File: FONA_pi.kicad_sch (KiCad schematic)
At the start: 26 parts, among them J1 Conn_01x20_Socket, J10 Conn_01x04_Pin, J11 Conn_01x20_Socket, J12 Conn_01x20_Socket, J13 Conn_01x06_Socket, J14 Conn_01x06_Socket, J15 Conn_01x06_Socket, J16 Conn_01x06_Socket, J17 Conn_01x06_Socket, J2 Conn_02x20_Odd_Even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

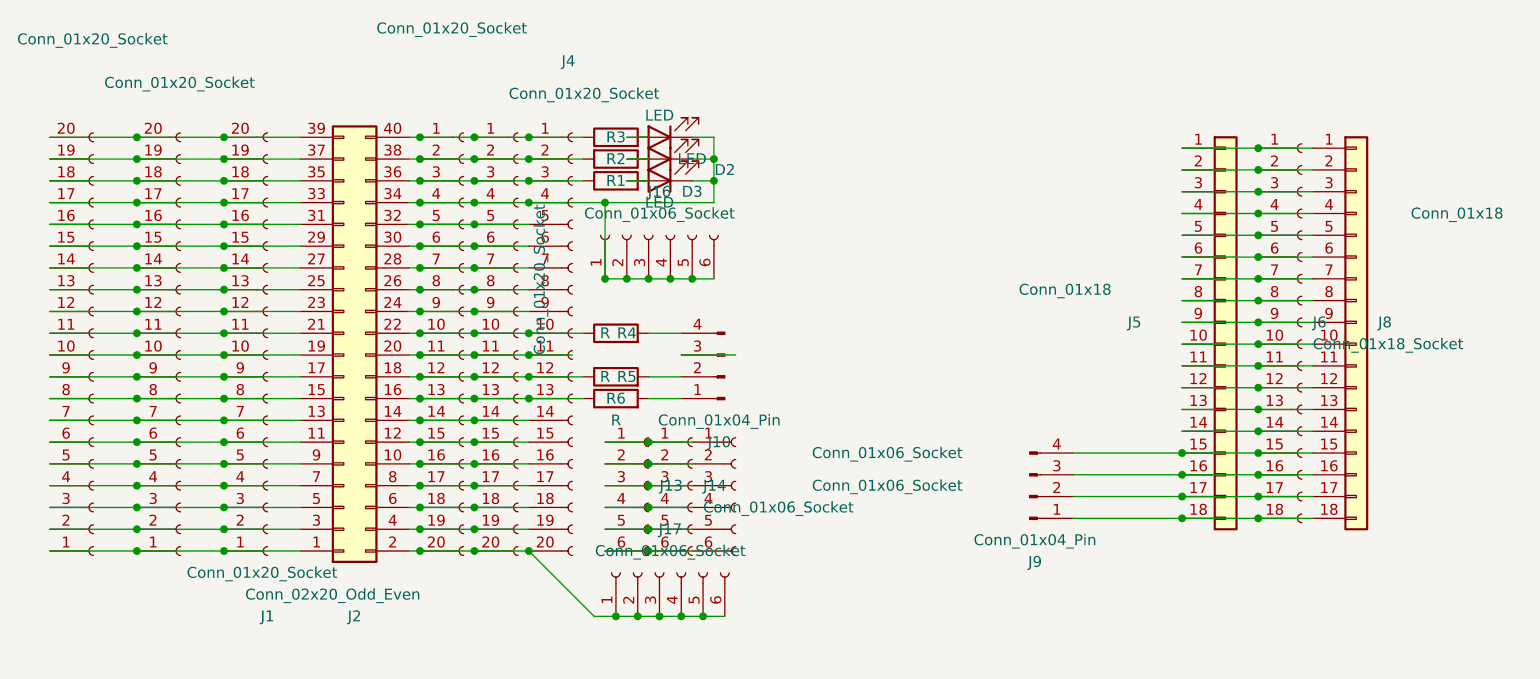
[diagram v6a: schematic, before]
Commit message: Added solder jumpers, ran them to GPIO pins.  Connected FONA pins to Pi, UART RX/TX, RI, NS, PS, etc to various GPIOs
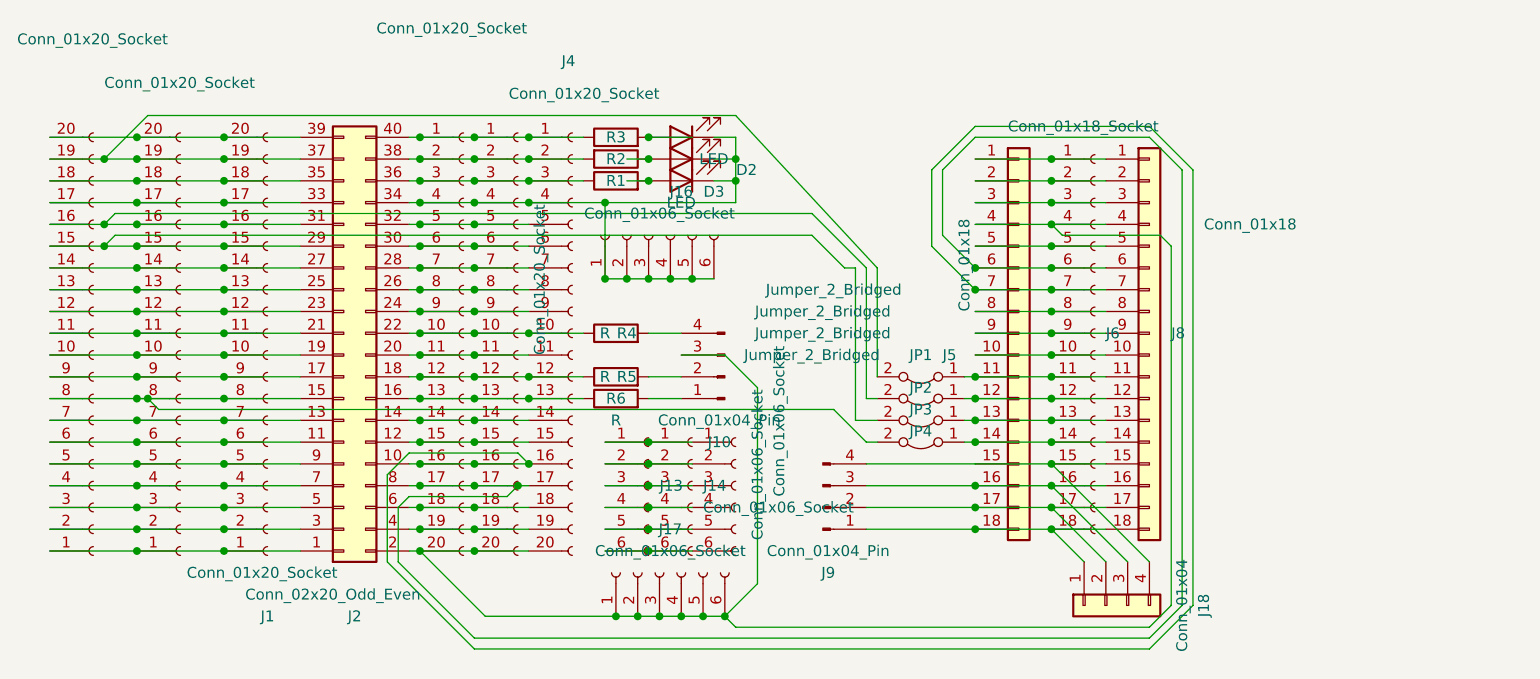
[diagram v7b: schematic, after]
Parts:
- added J18: Conn_01x04, Connector_Wago:Wago_734-134_1x04_P3.50mm_Vertical, symbol Connector_Generic:Conn_01x04
- added JP1, JP2, JP3, JP4: Jumper_2_Bridged, Jumper:SolderJumper-2_P1.3mm_Bridged_RoundedPad1.0x1.5mm, symbol Jumper:Jumper_2_Bridged
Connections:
- net at J2.10 (Pin_10), J3.16 (Pin_16), J4.16 (Pin_16)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: now also J5.7 (Pin_7), J6.7 (Pin_7), J8.7 (Pin_7)
- net at J2.8 (Pin_8), J3.17 (Pin_17), J4.17 (Pin_17)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: now also J5.6 (Pin_6), J6.6 (Pin_6), J8.6 (Pin_6)
- net at J17.1 (Pin_1), J17.2 (Pin_2), J17.3 (Pin_3)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: now also J10.3 (Pin_3), J5.4 (Pin_4), J6.4 (Pin_4), J8.4 (Pin_4)
- net at J1.15 (Pin_15), J11.15 (Pin_15), J12.15 (Pin_15)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: now also JP3.2 (B)
- net at J1.16 (Pin_16), J11.16 (Pin_16), J12.16 (Pin_16)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: now also JP2.2 (B)
- net at J1.19 (Pin_19), J11.19 (Pin_19), J12.19 (Pin_19)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: now also JP1.2 (B)
- net at J1.8 (Pin_8), J11.8 (Pin_8), J12.8 (Pin_8)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: now also JP4.2 (B)
- net at J5.11 (Pin_11), J6.11 (Pin_11), J8.11 (Pin_11): now also JP1.1 (A)
- net at J5.12 (Pin_12), J6.12 (Pin_12), J8.12 (Pin_12): now also JP2.1 (A)
- net at J5.13 (Pin_13), J6.13 (Pin_13), J8.13 (Pin_13): now also JP3.1 (A)
- net at J5.14 (Pin_14), J6.14 (Pin_14), J8.14 (Pin_14): now also JP4.1 (A)
- net at J5.15 (Pin_15), J6.15 (Pin_15), J8.15 (Pin_15)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: now also J18.4 (Pin_4)
- net at J5.16 (Pin_16), J6.16 (Pin_16), J8.16 (Pin_16)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: now also J18.3 (Pin_3)
- net at J5.17 (Pin_17), J6.17 (Pin_17), J8.17 (Pin_17)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: now also J18.2 (Pin_2)
- net at J5.18 (Pin_18), J6.18 (Pin_18), J8.18 (Pin_18)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: now also J18.1 (Pin_1)
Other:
- moved on the sheet: D2, D3, J5, J6, J8, J9

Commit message: Changed GPIO pins, so that no multi-purpose (UART/SPI/I2C) pins are used by default by the FONA, LEDs or switch connector, to keep them free for those uses
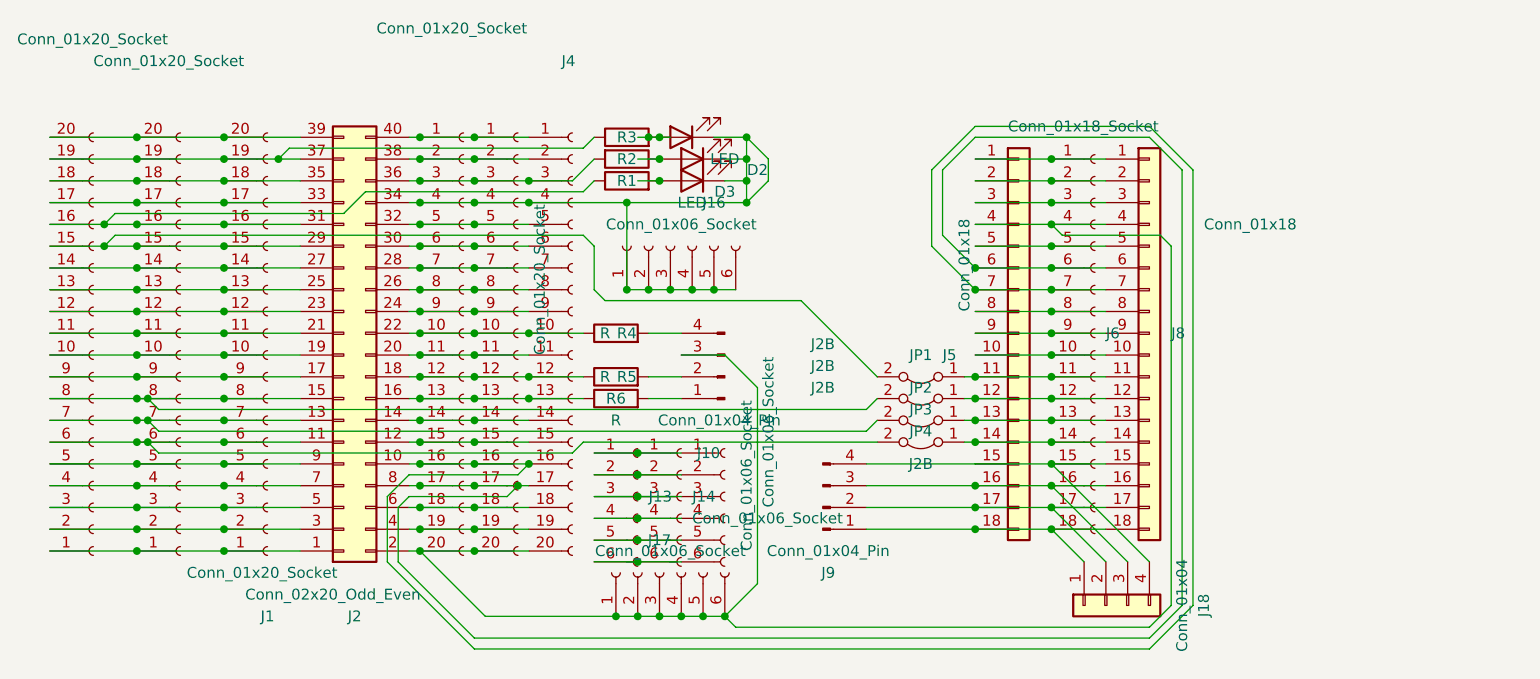
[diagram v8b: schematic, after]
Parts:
- JP1, JP2, JP3, JP4: value Jumper_2_Bridged -> J2B
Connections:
- net at J2.40 (Pin_40), J3.1 (Pin_1), J4.1 (Pin_1)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: no longer R3.1
- net at J2.38 (Pin_38), J3.2 (Pin_2), J4.2 (Pin_2)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: no longer R2.2
- net at J2.36 (Pin_36), J3.3 (Pin_3), J4.3 (Pin_3)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: now also R2.2; no longer R1.1
- net at J1.19 (Pin_19), J11.19 (Pin_19), J12.19 (Pin_19)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: now also R3.1; no longer JP1.2 (B)
- net at J1.15 (Pin_15), J11.15 (Pin_15), J12.15 (Pin_15)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: now also JP1.2 (B); no longer JP3.2 (B)
- net at J1.16 (Pin_16), J11.16 (Pin_16), J12.16 (Pin_16)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: now also R1.1; no longer JP2.2 (B)
- net at J1.6 (Pin_6), J11.6 (Pin_6), J12.6 (Pin_6)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: now also JP4.2 (B)
- net at J1.7 (Pin_7), J11.7 (Pin_7), J12.7 (Pin_7)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: now also JP3.2 (B)
- net at J1.8 (Pin_8), J11.8 (Pin_8), J12.8 (Pin_8)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: now also JP2.2 (B); no longer JP4.2 (B)
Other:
- moved on the sheet: D2, D3, J13, J14, J16, R1, R2, R3
